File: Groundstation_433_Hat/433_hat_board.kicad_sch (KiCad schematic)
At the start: 14 parts, among them J1 Conn_01x13_Pin, J2 Amphenol_901-144, Q1 2N7002, Q2 2N7002, U2 Raspberry_Pi_4B, U3 RFM96W

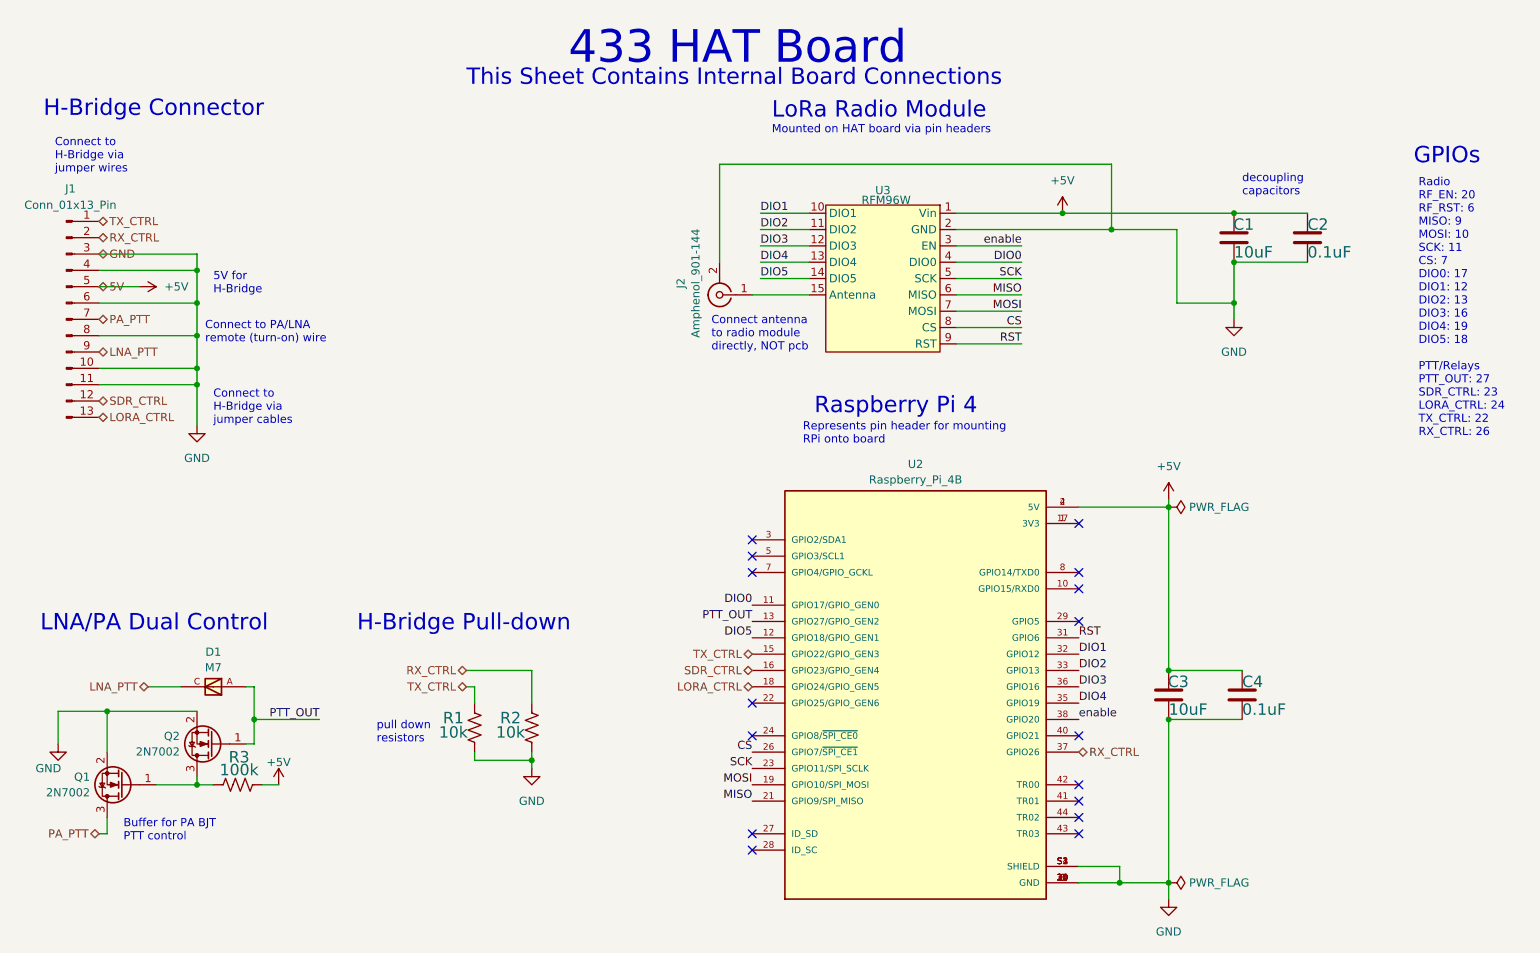
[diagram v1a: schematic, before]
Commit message: Updated Groundstation 433 Hat to KiCad 9
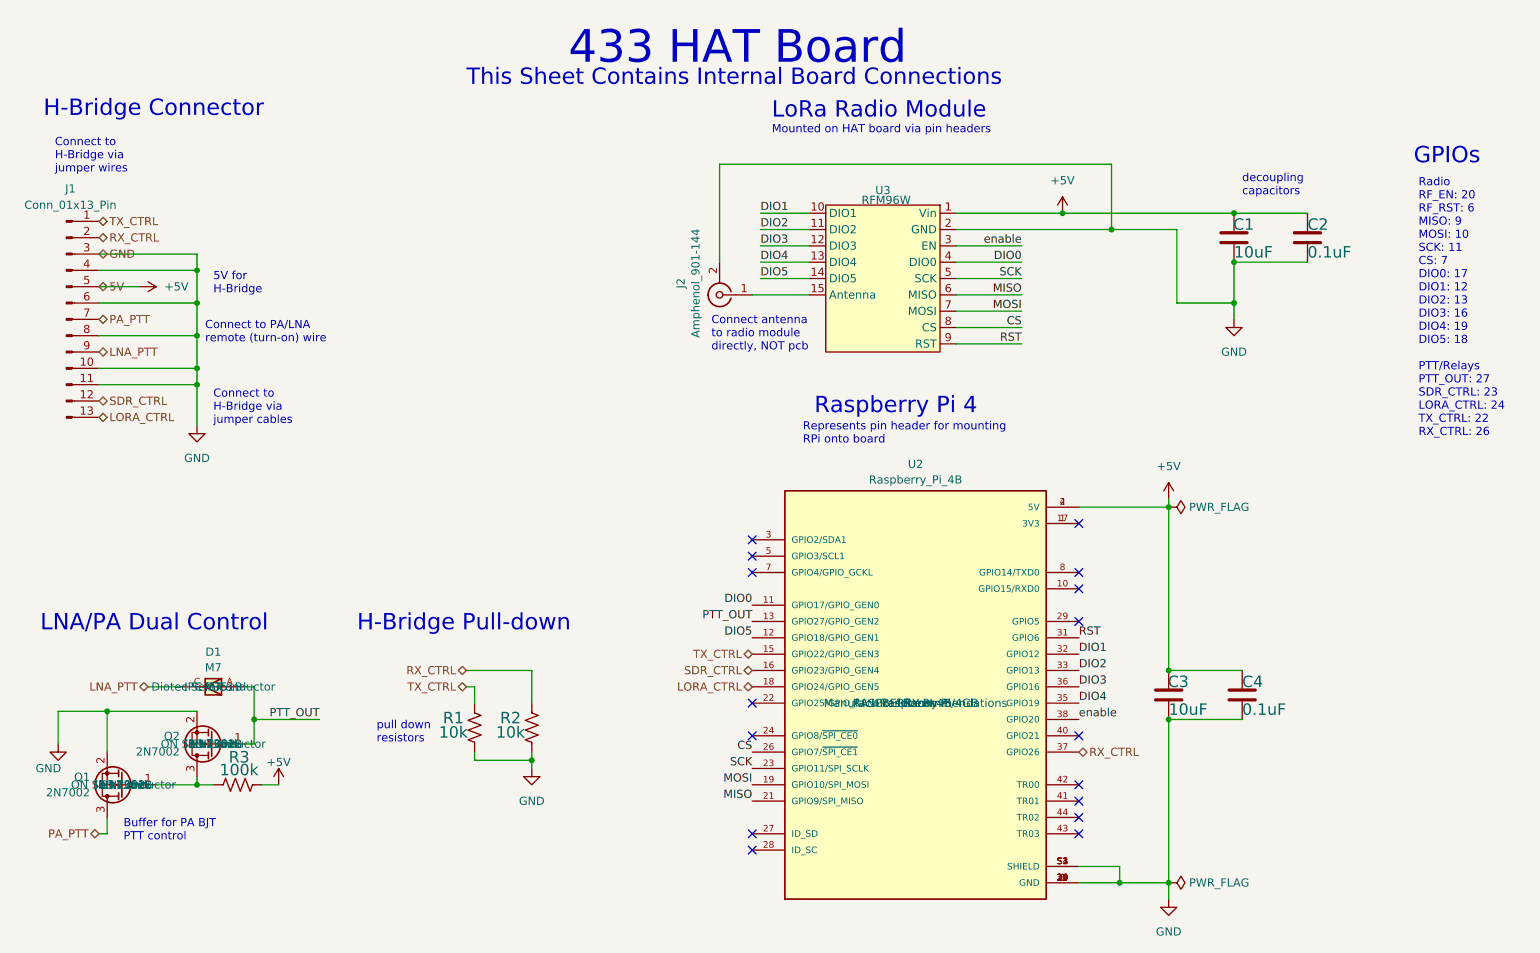
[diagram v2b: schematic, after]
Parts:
- D1: AVAILABILITY Not in stock -> (none); Availability In Stock -> (none); Check_prices https://www.snapeda.com/parts/M7/Diotec/view-part/?ref=eda -> (none); MANUFACTURER DIODES -> (none); MF Diotec Semiconductor -> (none); MP M7 -> (none); MPN M7 -> (none); Manufacturer_Name (none) -> Diotec Semiconductor; Manufacturer_Part_Number (none) -> M7; PACKAGE DO-214 -> (none); PARTREV NA -> (none); PRICE -- -> (none); Package Package -> (none); Price None -> (none); Purchase-URL https://www.snapeda.com/api/url_track_click_mouser/?unipart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 -> (none); SNAPEDA_PACKAGE_ID 7518 -> (none); STANDARD IPC-7351B -> (none); SnapEDA_Link https://www.snapeda.com/parts/M7/Diotec/view-part/?ref=snap -> (none); Standard (none) -> IPC-7351B
- J2: Flight 901-144 -> (none)
- Q1, Q2: Availability In Stock -> (none); Check_prices https://www.snapeda.com/parts/2N7002/Onsemi/view-part/?ref=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 -> (none); Height (none) -> 1.11 mm; MANUFACTURER ON Semiconductor -> (none); MAXIMUM_PACKAGE_HEIGHT 1.11 mm -> (none); MF ON Semiconductor -> (none); MP 2N7002 -> (none); Manufacturer_Name (none) -> ON Semiconductor; Manufacturer_Part_Number (none) -> 2N7002; PARTREV 4 -> (none); Package SOT-23-3 ON Semiconductor -> (none); Price None -> (none); Purchase-URL https://www.snapeda.com/api/url_track_click_mouser/?unipart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 -> (none); STANDARD IPC 7351B -> (none); SnapEDA_Link https://www.snapeda.com/parts/2N7002/Onsemi/view-part/?ref=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 -> (none); Standard (none) -> IPC 7351B
- U2: Availability Not in stock -> (none); Check_prices https://www.snapeda.com/parts/RASPBERRY%20PI%204B/4GB/Raspb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 -> (none); Height (none) -> 16 mm; MANUFACTURER Raspberry Pi -> (none); MAXIMUM_PACKAGE_HEIGHT 16 mm -> (none); MF Raspberry Pi -> (none); MP RASPBERRY PI 4B/4GB -> (none); Manufacturer_Name (none) -> Raspberry Pi; Manufacturer_Part_Number (none) -> RASPBERRY PI 4B/4GB; PARTREV 4 -> (none); Package None -> (none); Price None -> (none); SNAPEDA_PN RASPBERRY PI 4B/4GB -> (none); STANDARD Manufacturer Recommendations -> (none); SnapEDA_Link https://www.snapeda.com/parts/RASPBERRY%20PI%204B/4GB/Raspb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 -> (none); Standard (none) -> Manufacturer Recommendations
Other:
- company: (none) -> Stanford Student Space Initiative
- title: 433 HAT Board Internal Connections -> 433MHz Ground Station Board
